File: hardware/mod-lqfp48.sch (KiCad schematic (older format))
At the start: 2 parts, among them J1 Target, U1 STM32F103C8Tx

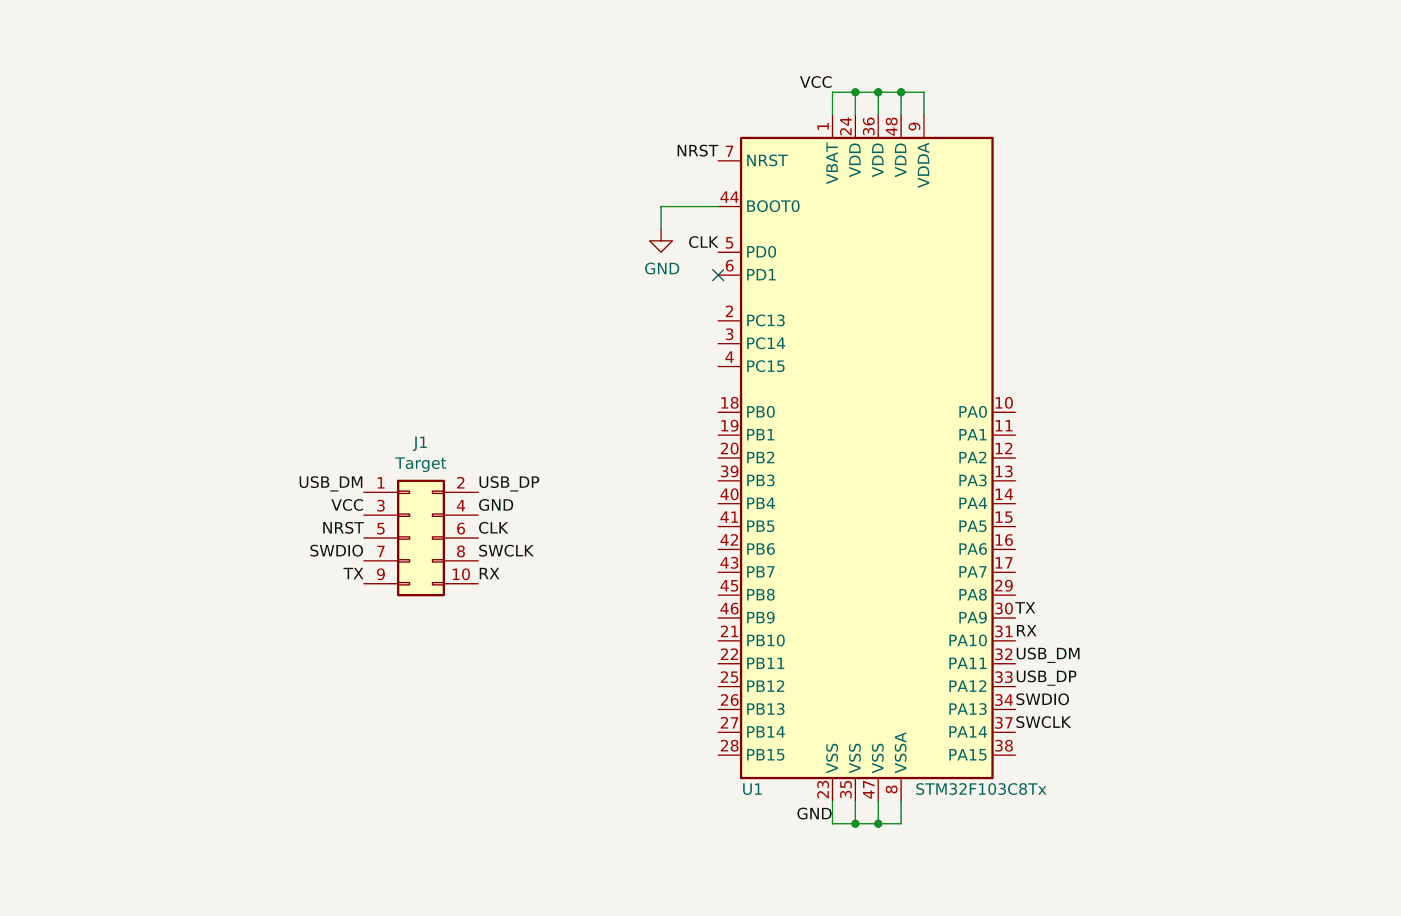
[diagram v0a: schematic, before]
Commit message: mod-lqfp48 board schematic finished
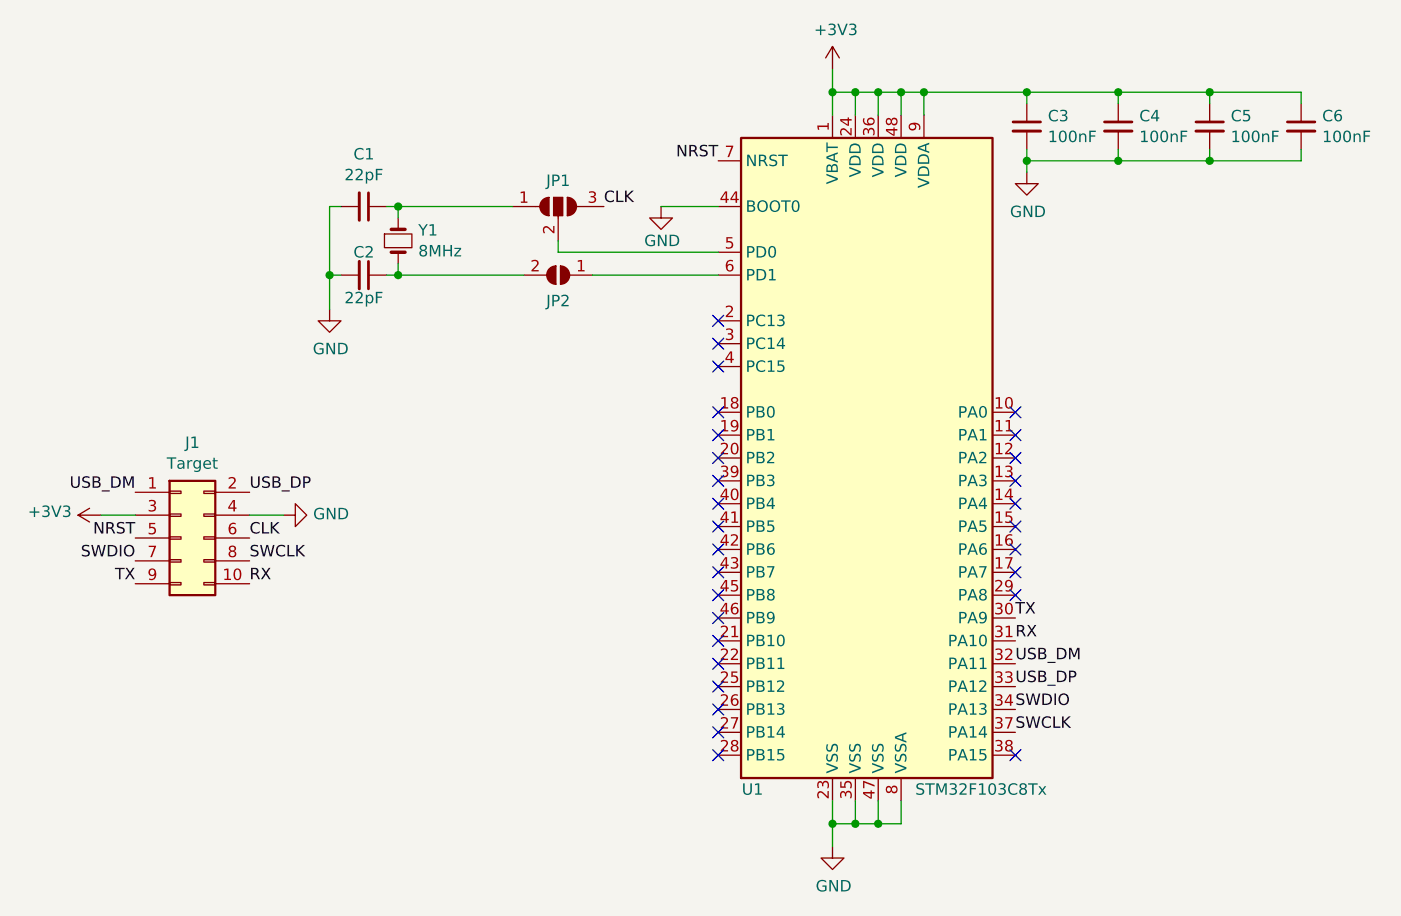
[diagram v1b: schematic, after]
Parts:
- added C1, C2: 22pF, symbol Device:C_Small
- added C3, C4, C5, C6: 100nF, symbol Device:C_Small
- added JP1: SolderJumper_3_Open, symbol Jumper:SolderJumper_3_Open
- added JP2: SolderJumper_2_Open, symbol Jumper:SolderJumper_2_Open
- added Y1: 8MHz, symbol Device:Crystal_Small
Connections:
- net CLK: now also JP1.3 (B); no longer U1.5 (PD0)
- net GND: now also C1.2, C2.2, C3.2, C4.2, C5.2, C6.2
- net at U1.6 (PD1): now also JP2.1 (A)
- net VCC renamed +3V3
- net +3V3: now also C3.1, C4.1, C5.1, C6.1
- new net: JP1.2 (C), U1.5 (PD0)
- new net: C1.1, JP1.1 (A), Y1.1
- new net: C2.1, JP2.2 (B), Y1.2
- no-connect marks 1 -> 29
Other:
- moved on the sheet: J1

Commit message: mod-lqfp48 board WIP
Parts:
- C1, C2, C3, C4, C5, C6: footprint (none) -> Capacitor_SMD:C_0805_2012Metric_Pad1.15x1.40mm_HandSolder
- JP1: footprint (none) -> Jumper:SolderJumper-3_P2.0mm_Open_TrianglePad1.0x1.5mm
- JP2: footprint (none) -> Jumper:SolderJumper-2_P1.3mm_Open_TrianglePad1.0x1.5mm
- Y1: footprint (none) -> Crystal:Crystal_HC18-U_Vertical
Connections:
- net RX: now also J1.2 (Pin_2); no longer J1.10 (Pin_10)
- net SWCLK: now also J1.7 (Pin_7); no longer J1.8 (Pin_8)
- net SWDIO: now also J1.8 (Pin_8); no longer J1.7 (Pin_7)
- net TX: now also J1.1 (Pin_1); no longer J1.9 (Pin_9)
- net USB_DM renamed USB_D-
- net USB_D-: now also J1.10 (Pin_10); no longer J1.1 (Pin_1)
- net USB_DP renamed USB_D+
- net USB_D+: now also J1.9 (Pin_9); no longer J1.2 (Pin_2)
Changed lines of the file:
@@
 	1    0    0    -1
 $EndComp
-Text Label 1850 3550 0    50   ~ 0
-USB_DP
-Text Label 1350 3550 2    50   ~ 0
-USB_DM
+Text Label 1850 3950 0    50   ~ 0
+USB_D-
+Text Label 1350 3950 2    50   ~ 0
+USB_D+
 Text Label 1850 3750 0    50   ~ 0
 CLK
-Text Label 1850 3850 0    50   ~ 0
-SWCLK
 Text Label 1350 3750 2    50   ~ 0
 NRST
-Text Label 1350 3850 2    50   ~ 0
+Text Label 1850 3850 0    50   ~ 0
 SWDIO
-Text Label 1350 3950 2    50   ~ 0
+Text Label 1350 3550 2    50   ~ 0
 TX
-Text Label 1850 3950 0    50   ~ 0
+Text Label 1850 3550 0    50   ~ 0
 RX
 $Comp
@@
 	4500 5000 4600 5000
 Text Label 5200 4300 0    50   ~ 0
-USB_DM
+USB_D-
 Text Label 5200 4400 0    50   ~ 0
-USB_DP
+USB_D+
 Text Label 5200 4500 0    50   ~ 0
 SWDIO
@@
 F 0 "Y1" V 2454 2538 50  0000 L CNN
 F 1 "8MHz" V 2545 2538 50  0000 L CNN
-F 2 "" H 2500 2450 50  0001 C CNN
+F 2 "Crystal:Crystal_HC18-U_Vertical" H 2500 2450 50  0001 C CNN
 F 3 "~" H 2500 2450 50  0001 C CNN
 	1    2500 2450
@@
 F 0 "C1" V 2121 2300 50  0000 C CNN
 F 1 "22pF" V 2212 2300 50  0000 C CNN
-F 2 "" H 2350 2300 50  0001 C CNN
+F 2 "Capacitor_SMD:C_0805_2012Metric_Pad1.15x1.40mm_HandSolder" H 2350 2300 50  0001 C CNN
 F 3 "~" H 2350 2300 50  0001 C CNN
 	1    2350 2300
@@
 F 0 "C2" V 2250 2600 50  0000 C CNN
 F 1 "22pF" V 2450 2600 50  0000 C CNN
-F 2 "" H 2350 2600 50  0001 C CNN
+F 2 "Capacitor_SMD:C_0805_2012Metric_Pad1.15x1.40mm_HandSolder" H 2350 2600 50  0001 C CNN
 F 3 "~" H 2350 2600 50  0001 C CNN
 	1    2350 2600
@@
 F 0 "JP1" H 3200 2413 50  0000 C CNN
 F 1 "SolderJumper_3_Open" V 3155 2367 50  0001 L CNN
-F 2 "" H 3200 2300 50  0001 C CNN
+F 2 "Jumper:SolderJumper-3_P2.0mm_Open_TrianglePad1.0x1.5mm" H 3200 2300 50  0001 C CNN
 F 3 "~" H 3200 2300 50  0001 C CNN
 	1    3200 2300
@@
 F 0 "JP2" H 3200 2713 50  0000 C CNN
 F 1 "SolderJumper_2_Open" V 3245 2668 50  0001 L CNN
-F 2 "" H 3200 2600 50  0001 C CNN
+F 2 "Jumper:SolderJumper-2_P1.3mm_Open_TrianglePad1.0x1.5mm" H 3200 2600 50  0001 C CNN
 F 3 "~" H 3200 2600 50  0001 C CNN
 	1    3200 2600
@@
 F 0 "C3" H 5342 1996 50  0000 L CNN
 F 1 "100nF" H 5342 1905 50  0000 L CNN
-F 2 "" H 5250 1950 50  0001 C CNN
+F 2 "Capacitor_SMD:C_0805_2012Metric_Pad1.15x1.40mm_HandSolder" H 5250 1950 50  0001 C CNN
 F 3 "~" H 5250 1950 50  0001 C CNN
 	1    5250 1950
@@
 F 0 "C4" H 5742 1996 50  0000 L CNN
 F 1 "100nF" H 5742 1905 50  0000 L CNN
-F 2 "" H 5650 1950 50  0001 C CNN
+F 2 "Capacitor_SMD:C_0805_2012Metric_Pad1.15x1.40mm_HandSolder" H 5650 1950 50  0001 C CNN
 F 3 "~" H 5650 1950 50  0001 C CNN
 	1    5650 1950
@@
 F 0 "C5" H 6142 1996 50  0000 L CNN
 F 1 "100nF" H 6142 1905 50  0000 L CNN
-F 2 "" H 6050 1950 50  0001 C CNN
+F 2 "Capacitor_SMD:C_0805_2012Metric_Pad1.15x1.40mm_HandSolder" H 6050 1950 50  0001 C CNN
 F 3 "~" H 6050 1950 50  0001 C CNN
 	1    6050 1950
@@
 F 0 "C6" H 6542 1996 50  0000 L CNN
 F 1 "100nF" H 6542 1905 50  0000 L CNN
-F 2 "" H 6450 1950 50  0001 C CNN
+F 2 "Capacitor_SMD:C_0805_2012Metric_Pad1.15x1.40mm_HandSolder" H 6450 1950 50  0001 C CNN
 F 3 "~" H 6450 1950 50  0001 C CNN
 	1    6450 1950
@@
 Wire Wire Line
 	2000 3650 1850 3650
+Text Label 1350 3850 2    50   ~ 0
+SWCLK
 $EndSCHEMATC
